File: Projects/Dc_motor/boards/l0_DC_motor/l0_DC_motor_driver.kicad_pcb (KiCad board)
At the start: 2 copper layers, 20.3 x 15.2 mm, 16 parts, among them J1 l0_Socket, J2 1776275-2, J3 1776275-2, Q1 PMV25ENEA, U1 DRV8833, U2 LMV301

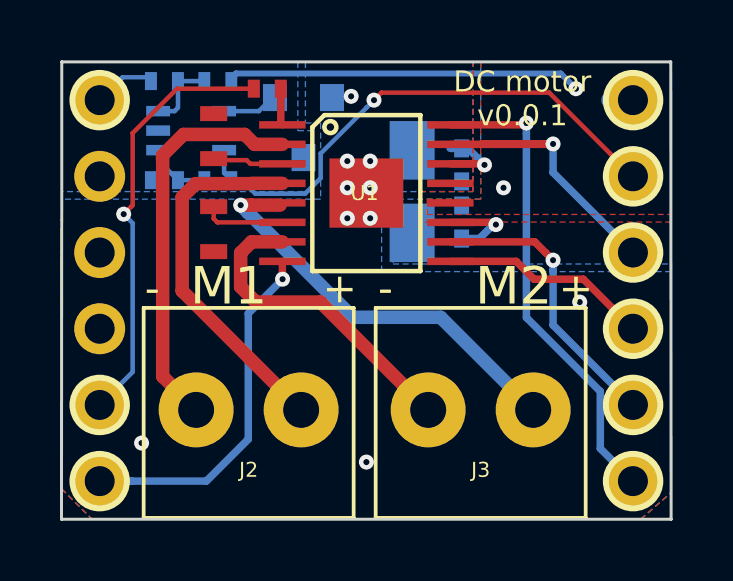
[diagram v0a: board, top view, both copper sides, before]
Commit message: change board kicad for project : Braekout board Luos Kit DC motor Servo
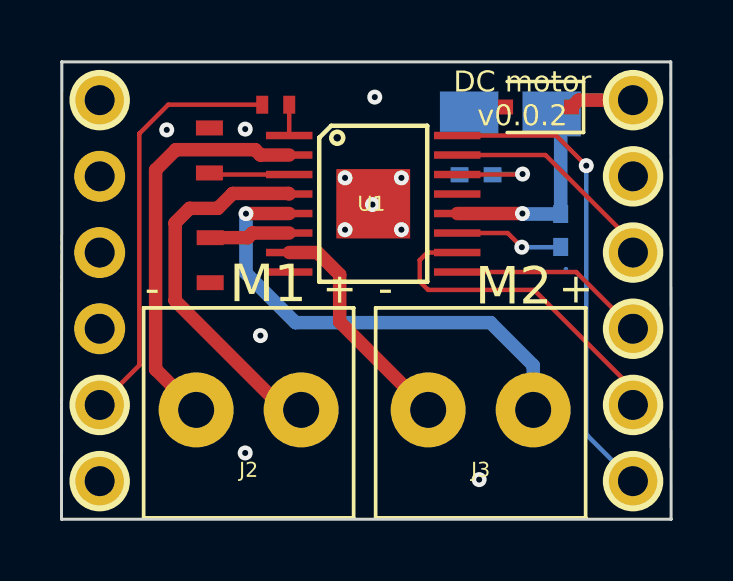
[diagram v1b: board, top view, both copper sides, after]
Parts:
- removed Q1: PMV25ENEA, Common_Footprint:SOT-23
- removed R4: 11.8K, Common_Footprint:R_0402_NoSilk
- removed R5, R7: 10K, Common_Footprint:R_0402_NoSilk
- removed R6: 68K, Common_Footprint:R_0402_NoSilk
- removed U2: LMV301, Common_Footprint:SC-70-5
- added D1: D_Zener, Common_Footprint:D_SOD-323F, F.Cu at (105.0, -7.14)
- J1: value l0_Socket -> l0_Shield_Socket
- moved C1 4.18 mm to (104.1, -6.91), turned to 180 degrees
- moved C2 3.31 mm to (105.8, -3.02)
- moved R2 1.04 mm to (94.1, -2.03)
- moved R1 0.60 mm to (96.3, -7.21)
- moved C3 0.58 mm to (103.0, -4.88), turned to 180 degrees
- moved R3 0.50 mm to (94.1, -5.69)
- moved U1 0.42 mm to (99.5, -3.91)
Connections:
- C1 pad 2: GNDPWR -> GND
- C3 pad 2: GNDPWR -> GND
- R2 pad 2: GNDPWR -> GND
- R3 pad 2: GNDPWR -> GND
- U1 pad 13: GNDPWR -> GND
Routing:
- net +3V3: track 17.7 -> 0.00 mm, vias 1 -> 0
- net /~nFAULT: track 11.9 -> 0.00 mm, vias 1 -> 0
- net Net-(R6-Pad2): track 2.47 -> 0.00 mm
- net /NO_PWM1: track 10.4 -> 8.25 mm, vias 1 -> 0
- net /Vmax: track 2.15 -> 0.00 mm
- net GND: track 2.08 -> 0.00 mm, vias 0 -> 11
- net /NO_PWM2: track 9.60 -> 11.7 mm, vias 1 -> 0
- net Net-(J3-Pad1): track 10.6 -> 8.64 mm
- net Net-(J3-Pad2): track 13.9 -> 15.8 mm
- net Net-(Q1-Pad1): track 1.65 -> 0.00 mm
- net Net-(J2-Pad2): track 12.2 -> 13.6 mm
- net /Robus_PS: track 12.6 -> 13.5 mm, vias 2 -> 1
- net Net-(C2-Pad2): track 2.88 -> 3.66 mm
- net Net-(C3-Pad1): track 2.52 -> 3.19 mm
- net /~nSLEEP: track 14.4 -> 14.6 mm, vias 1 -> 0
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- added copper zone on F.Cu, net GND
- removed copper zone on B.Cu, net /Robus_PS
- removed copper zone on F.Cu, net /Robus_PS
- removed copper zone on B.Cu, net GNDPWR
- removed copper zone on F.Cu, net GNDPWR
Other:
- board text added: "DC motor v0.0.2"
- board text removed: "DC motor v0.0.1"
